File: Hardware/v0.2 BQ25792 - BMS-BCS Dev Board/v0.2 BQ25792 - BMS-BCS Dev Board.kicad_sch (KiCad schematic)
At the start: 45 parts, among them J1 Barrel Jack, J2 Barrel Jack, J3 JST-VH Shrouded, J5 JST-PH, Q1 ACFET1, Q2 RBFET1, Q3 ACFET2, Q4 RBFET2, Q5 BATFET, U1 BQ25792RQMR

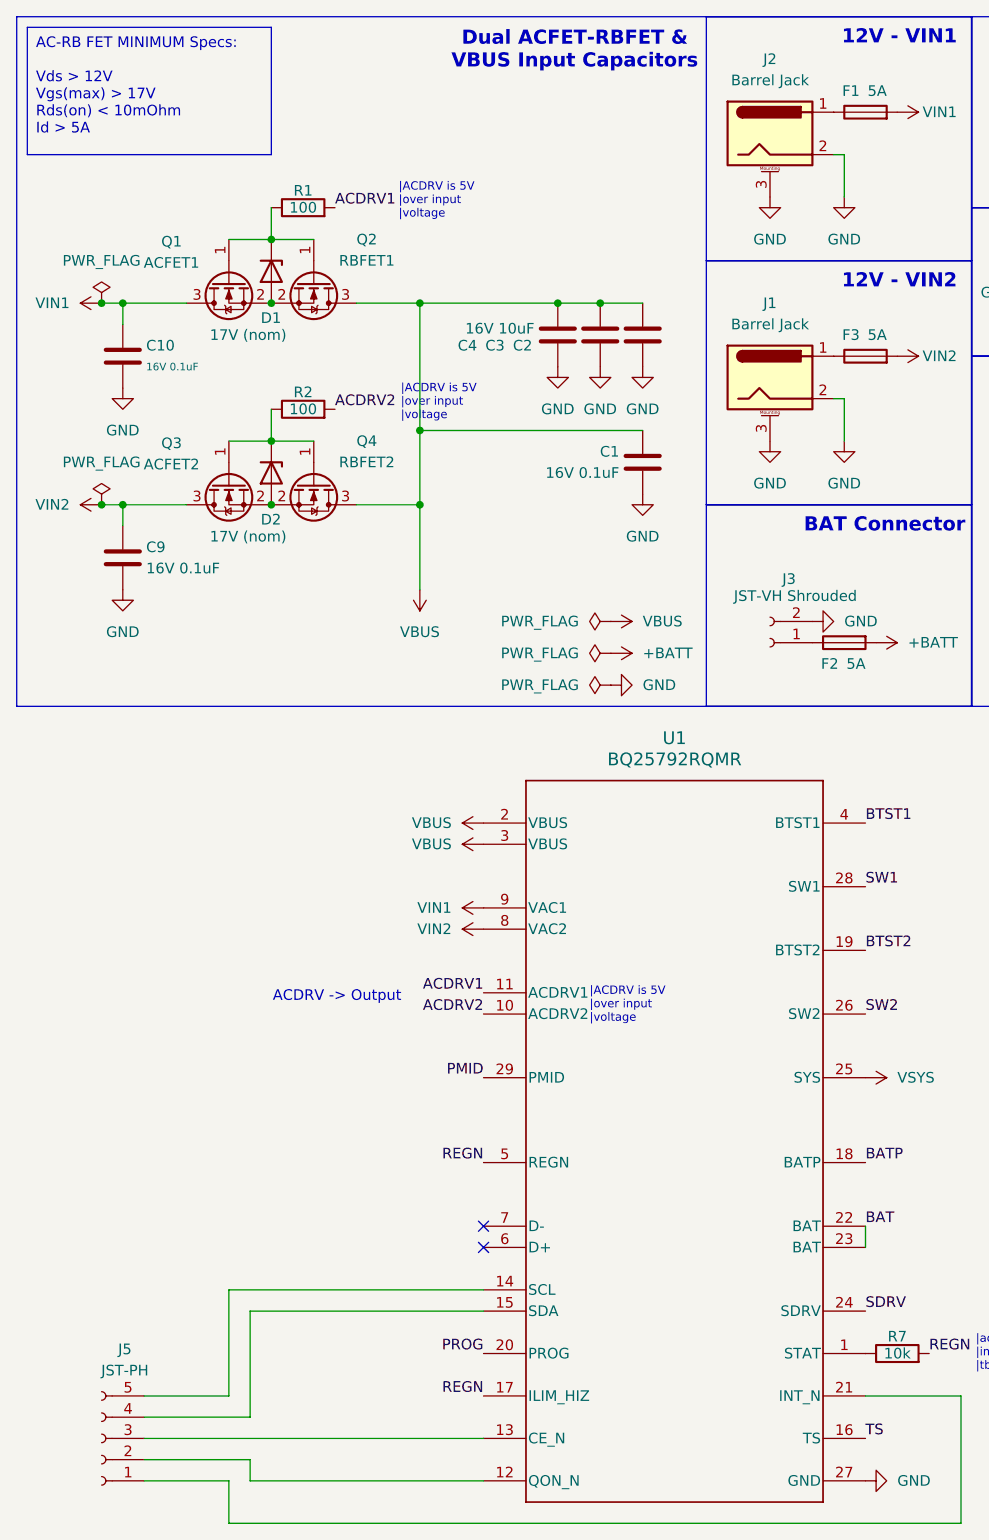
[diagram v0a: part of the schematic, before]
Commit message: BMS/BCS Ordering Preparations
Finished all ordering preparations, PCB in production.
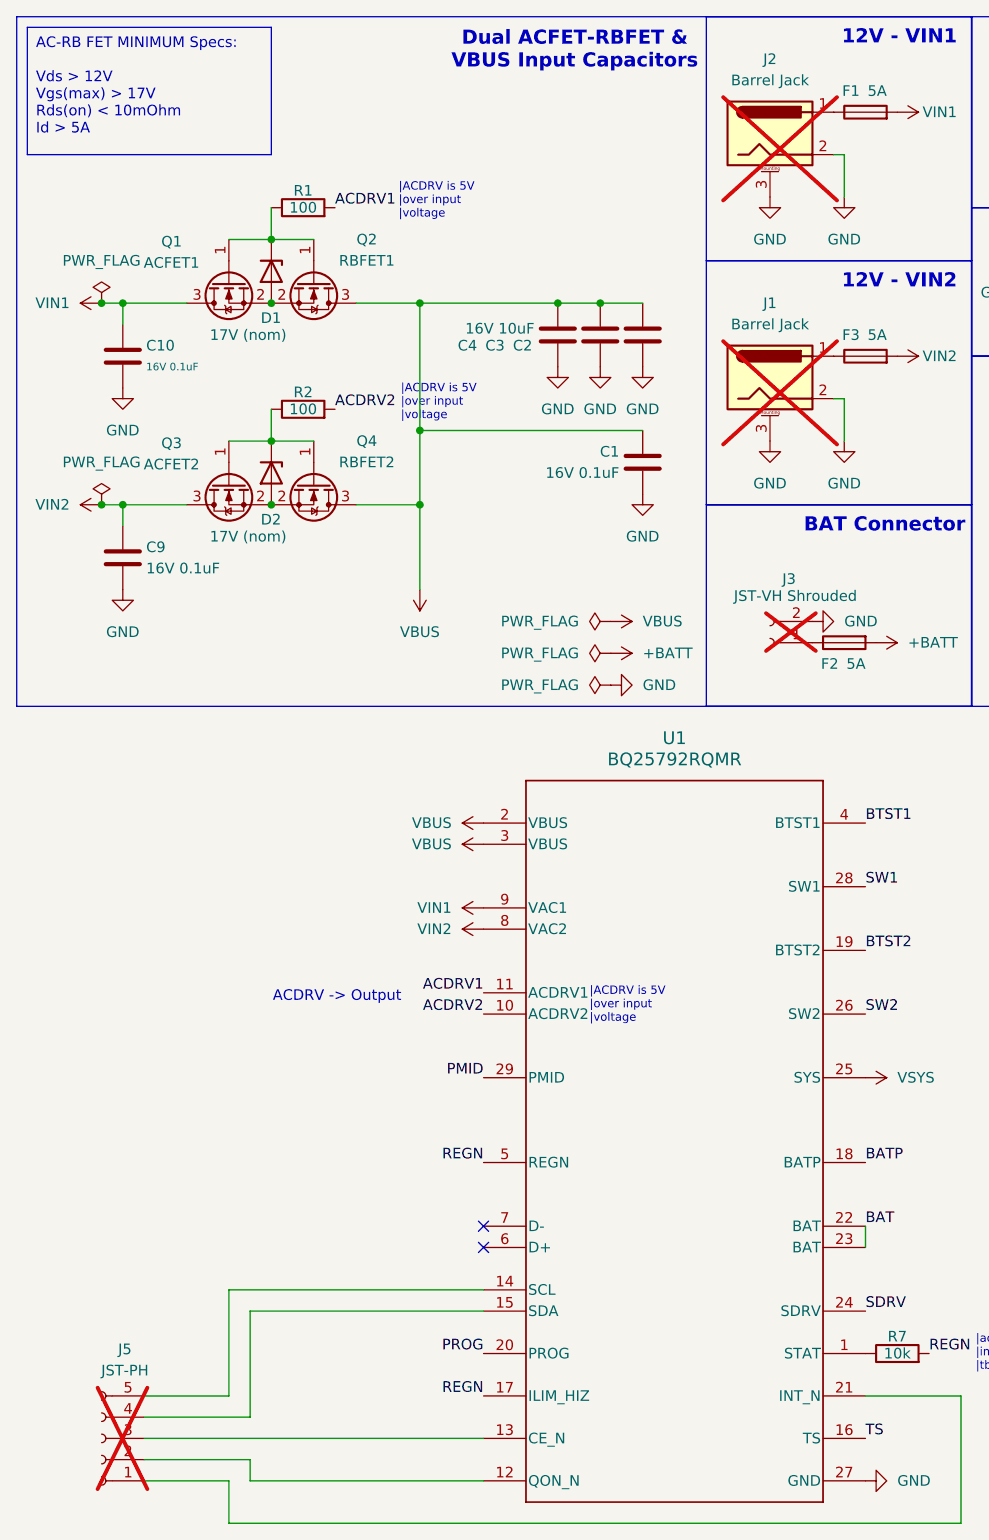
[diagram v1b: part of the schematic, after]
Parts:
- C1, C10, C14, C5, C9: LCSC Part Number (none) -> C22435940
- C11: LCSC Part Number (none) -> C466621
- C12, C13: LCSC Part Number (none) -> C5142571
- C15, C16, C17, C18, C19, C2, C20, C21, C3, C4, C6, C7, C8: LCSC Part Number (none) -> C7472961
- D1, D2: LCSC Part Number (none) -> C308704
- F1, F2, F3: LCSC Part Number (none) -> C206961
- J1, J2, J3, J5: now not fitted
- L1: LCSC Part Number (none) -> C22463806
- Q1, Q2, Q3, Q4: LCSC Part Number (none) -> C915719
- Q5: LCSC Part Number (none) -> C3033398
- R1, R2, R6: LCSC Part Number (none) -> C2906884
- R3: LCSC Part Number (none) -> C2929913
- R4: LCSC Part Number (none) -> C11631
- R5: LCSC Part Number (none) -> C4156287
- R7: LCSC Part Number (none) -> C2906885
- TH1: LCSC Part Number (none) -> C497233
- U1: LCSC Part Number (none) -> C2862876

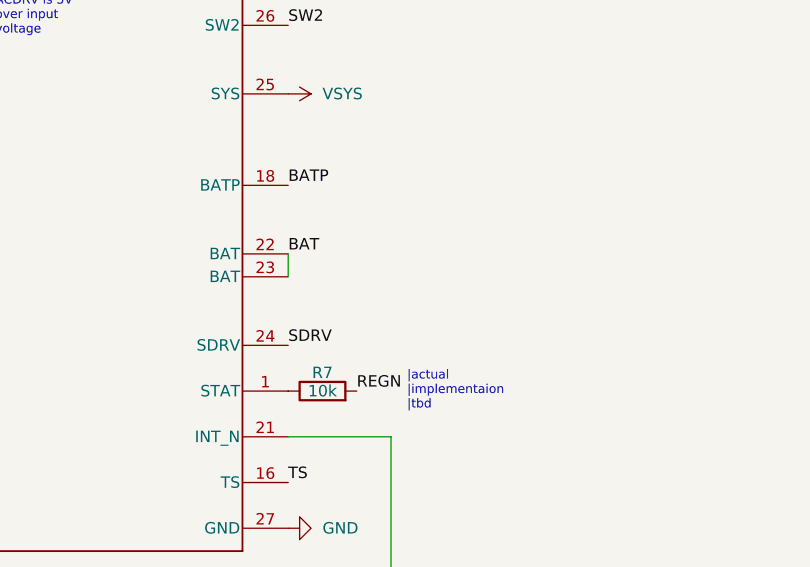
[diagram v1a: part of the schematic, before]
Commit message: BMS/BCS Board Modified
Added System Connector
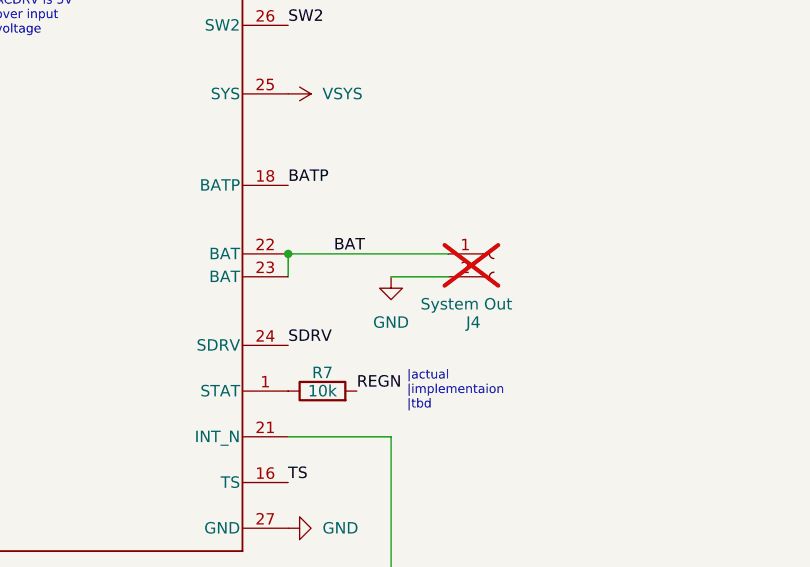
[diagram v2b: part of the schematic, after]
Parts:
- added J4: System Out, Connector_JST:JST_VH_B2P-VH-FB-B_1x02_P3.96mm_Vertical, symbol Connector:Conn_01x02_Socket
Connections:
- net BAT: now also J4.1 (Pin_1)
- net GND: now also J4.2 (Pin_2)
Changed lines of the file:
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@@
 	)
 	(junction
+		(at 120.65 157.48)
+		(diameter 0)
+		(color 0 0 0 0)
+	)
+	(junction
 		(at 67.31 62.23)
 		(diameter 0)
@@
 	(wire
 		(pts
+			(xy 138.43 160.02) (xy 132.08 160.02)
+		)
+		(stroke
+			(width 0)
+			(type default)
+		)
+	)
+	(wire
+		(pts
 			(xy 44.45 193.04) (xy 44.45 187.96)
 		)
@@
 	(wire
 		(pts
+			(xy 120.65 157.48) (xy 138.43 157.48)
+		)
+		(stroke
+			(width 0)
+			(type default)
+		)
+	)
+	(wire
+		(pts
 			(xy 49.53 59.69) (xy 49.53 63.5)
 		)
@@
 	)
 	(label "BAT"
-		(at 120.65 157.48 0)
+		(at 125.73 157.48 0)
 		(fields_autoplaced yes)
 		(effects
@@
 	)
 	(symbol
+		(lib_id "Connector:Conn_01x02_Socket")
+		(at 143.51 157.48 0)
+		(unit 1)
+		(exclude_from_sim no)
+		(in_bom yes)
+		(on_board yes)
+		(dnp yes)
+		(property "Reference" "J4"
+			(at 141.224 165.1 0)
+			(effects
+				(font
+					(size 1.27 1.27)
+				)
+			)
+		)
+		(property "Value" "System Out"
+			(at 140.462 163.068 0)
+			(effects
+				(font
+					(size 1.27 1.27)
+				)
+			)
+		)
+		(property "Footprint" "Connector_JST:JST_VH_B2P-VH-FB-B_1x02_P3.96mm_Vertical"
+			(at 143.51 157.48 0)
+			(effects
+				(font
+					(size 1.27 1.27)
+				)
+				(hide yes)
+			)
+		)
+		(property "Datasheet" "~"
+			(at 143.51 157.48 0)
+			(effects
+				(font
+					(size 1.27 1.27)
+				)
+				(hide yes)
+			)
+		)
+		(property "Description" "Generic connector, single row, 01x02, script generated"
+			(at 143.51 157.48 0)
+			(effects
+				(font
+					(size 1.27 1.27)
+				)
+				(hide yes)
+			)
+		)
+		(property "LCSC Part Number" ""
+			(at 143.51 157.48 0)
+			(effects
+				(font
+					(size 1.27 1.27)
+				)
+				(hide yes)
+			)
+		)
+		(pin "2"
+		)
+		(pin "1"
+		)
+		(instances
+			(project "v0.2 BQ25792 - BMS-BCS Dev Board"
+				(path "/9e49e097-8a55-4650-afb3-621b68b72b0d"
+					(reference "J4")
+					(unit 1)
+				)
+			)
+		)
+	)
+	(symbol
 		(lib_id "power:+12VA")
 		(at 29.21 46.99 90)
@@
 					(unit 1)
 				)
+			)
+		)
+	)
+	(symbol
+		(lib_id "power:GND")
+		(at 132.08 160.02 0)
+		(unit 1)
+		(exclude_from_sim no)
+		(in_bom yes)
+		(on_board yes)
+		(dnp no)
+		(fields_autoplaced yes)
+		(property "Reference" "#PWR042"
+			(at 132.08 166.37 0)
+			(effects
+				(font
+					(size 1.27 1.27)
+				)
+				(hide yes)
+			)
+		)
+		(property "Value" "GND"
+			(at 132.08 165.1 0)
+			(effects
+				(font
+					(size 1.27 1.27)
+				)
+			)
+		)
+		(property "Footprint" ""
+			(at 132.08 160.02 0)
+			(effects
+				(font
+					(size 1.27 1.27)
+				)
+				(hide yes)
+			)
+		)
+		(property "Datasheet" ""
+			(at 132.08 160.02 0)
+			(effects
+				(font
+					(size 1.27 1.27)
+				)
+				(hide yes)
+			)
+		)
+		(property "Description" "Power symbol creates a global label with name \"GND\" , ground"
+			(at 132.08 160.02 0)
+			(effects
+				(font
+					(size 1.27 1.27)
+				)
+				(hide yes)
+			)
+		)
+		(pin "1"
+		)
+		(instances
+			(project ""
+				(path "/9e49e097-8a55-4650-afb3-621b68b72b0d"
+					(reference "#PWR042")
+					(unit 1)
+				)
